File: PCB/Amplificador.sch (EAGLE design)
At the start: 36 parts, among them Q1 BC214, Q10 MJE2955, Q11 MJE3055, Q2 BC214, Q3 BC214, Q4 BC214, Q5 2N3904, Q6 2N3904, Q7 2N3904, Q8 2N3904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

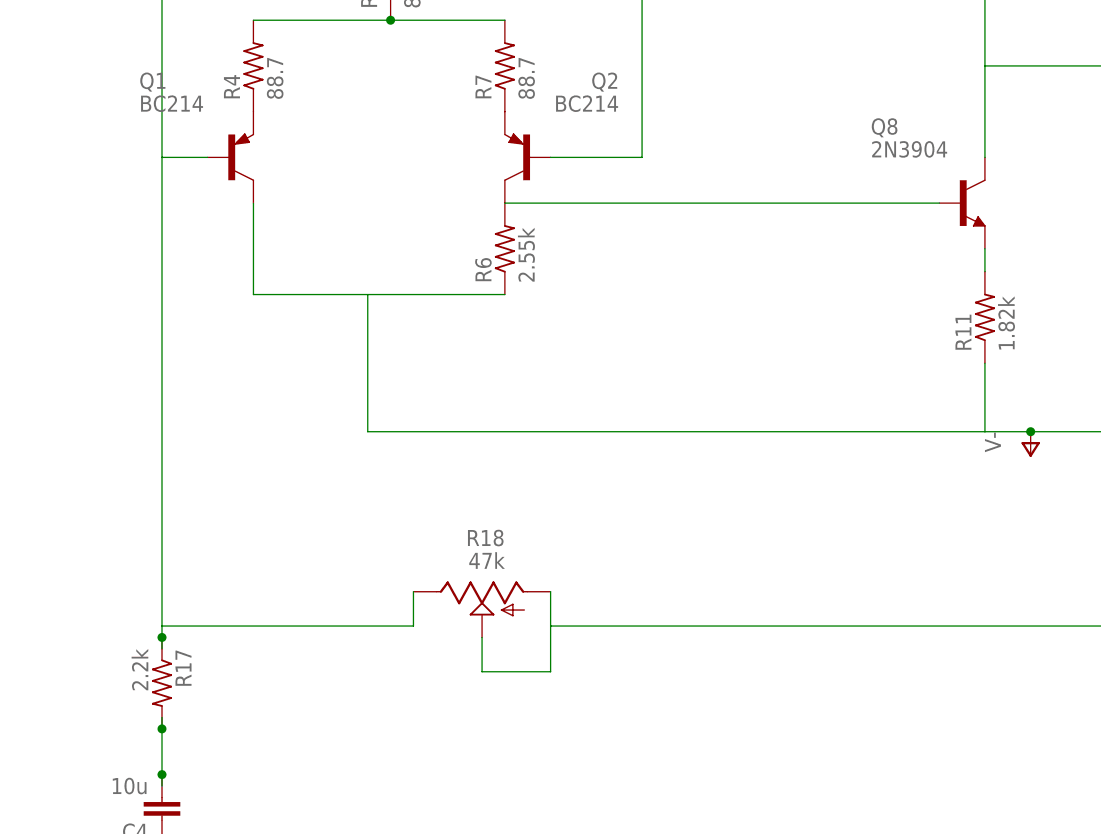
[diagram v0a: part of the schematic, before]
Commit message: Placa Versão 2.0
Talvez a versão final, compatível com nossos componentes comprados
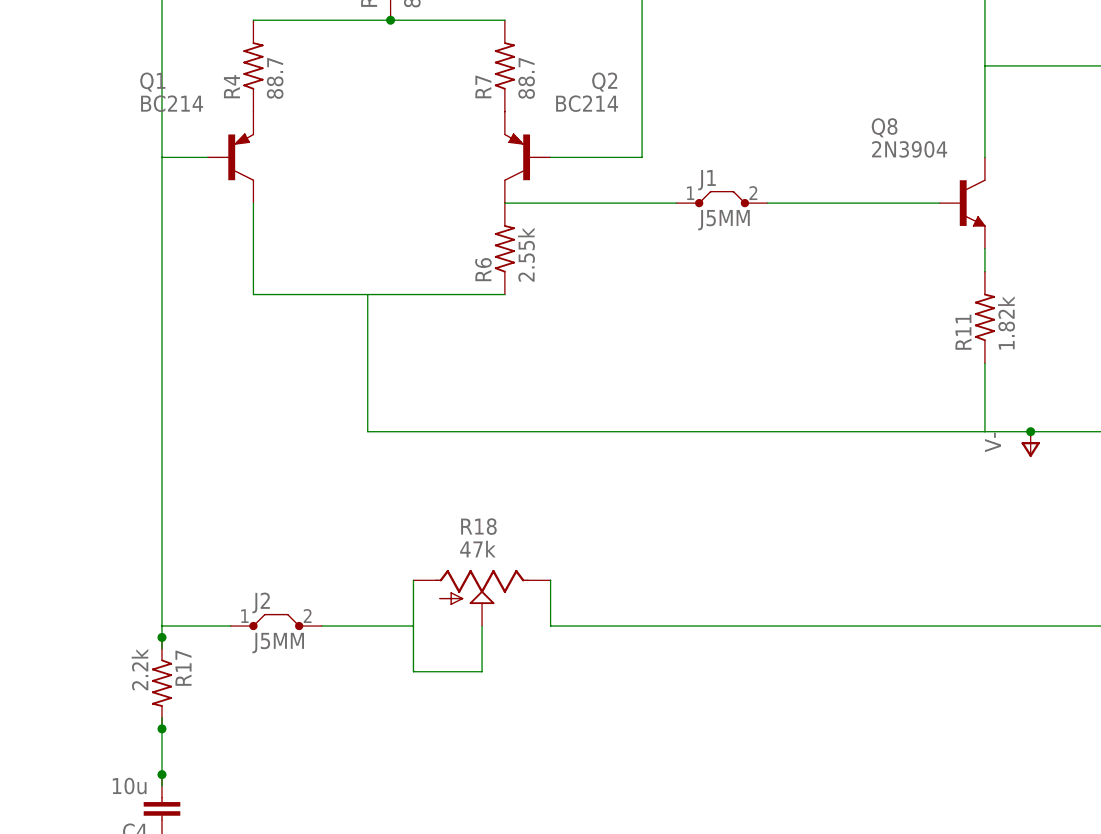
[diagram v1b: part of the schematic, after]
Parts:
- added J1, J2: J5MM, jumper:J5MM
- R18: device pot:TRIM_US-CA6V -> pot:TRIM_US-CA6H
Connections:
- new net N$25: J1.1, Q2.C, R6.2
- new net N$26: J2.1, Q1.B, Q5.B, R17.1
- net N$15: now also R18.E; no longer R18.A, R18.S
- net N$19: now also J2.2, R18.A, R18.S; no longer Q1.B, Q5.B, R17.1, R18.E
- net N$2: now also J1.2; no longer Q2.C, R6.2
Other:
- moved on the sheet: R18
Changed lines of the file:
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@@
 <setting verticaltext="up"/>
 </settings>
-<grid distance="0.1" unitdist="inch" unit="inch" style="lines" multiple="1" display="no" altdistance="0.01" altunitdist="inch" altunit="inch"/>
+<grid distance="0.05" unitdist="inch" unit="inch" style="lines" multiple="1" display="no" altdistance="0.01" altunitdist="inch" altunit="inch"/>
 <layers>
 <layer number="1" name="Top" color="4" fill="1" visible="no" active="no"/>
+<layer number="2" name="Route2" color="1" fill="3" visible="no" active="no"/>
+<layer number="3" name="Route3" color="4" fill="3" visible="no" active="no"/>
+<layer number="4" name="Route4" color="1" fill="4" visible="no" active="no"/>
+<layer number="5" name="Route5" color="4" fill="4" visible="no" active="no"/>
+<layer number="6" name="Route6" color="1" fill="8" visible="no" active="no"/>
+<layer number="7" name="Route7" color="4" fill="8" visible="no" active="no"/>
+<layer number="8" name="Route8" color="1" fill="2" visible="no" active="no"/>
+<layer number="9" name="Route9" color="4" fill="2" visible="no" active="no"/>
+<layer number="10" name="Route10" color="1" fill="7" visible="no" active="no"/>
+<layer number="11" name="Route11" color="4" fill="7" visible="no" active="no"/>
+<layer number="12" name="Route12" color="1" fill="5" visible="no" active="no"/>
+<layer number="13" name="Route13" color="4" fill="5" visible="no" active="no"/>
+<layer number="14" name="Route14" color="1" fill="6" visible="no" active="no"/>
+<layer number="15" name="Route15" color="4" fill="6" visible="no" active="no"/>
 <layer number="16" name="Bottom" color="1" fill="1" visible="no" active="no"/>
 <layer number="17" name="Pads" color="2" fill="1" visible="no" active="no"/>
@@
 <part name="GND4" library="supply1" library_urn="urn:adsk.eagle:library:371" deviceset="GND" device=""/>
 <part name="R17" library="resistor" library_urn="urn:adsk.eagle:library:348" deviceset="R-US_" device="0207/10" package3d_urn="urn:adsk.eagle:package:25939/1" value="2.2k"/>
-<part name="R18" library="pot" library_urn="urn:adsk.eagle:library:331" deviceset="TRIM_US-" device="CA6V" package3d_urn="urn:adsk.eagle:package:22691/1" value="47k"/>
 <part name="C4" library="capacitor-wima" library_urn="urn:adsk.eagle:library:116" deviceset="C" device="5/2.5" package3d_urn="urn:adsk.eagle:package:5426/1" value="10u"/>
 <part name="GND5" library="supply1" library_urn="urn:adsk.eagle:library:371" deviceset="GND" device=""/>
@@
 <part name="Q10" library="transistor-power" library_urn="urn:adsk.eagle:library:400" deviceset="MJE2955" device="" package3d_urn="urn:adsk.eagle:package:29487/1"/>
 <part name="Q11" library="transistor-power" library_urn="urn:adsk.eagle:library:400" deviceset="MJE3055" device="" package3d_urn="urn:adsk.eagle:package:29487/1"/>
+<part name="J1" library="jumper" library_urn="urn:adsk.eagle:library:252" deviceset="J" device="5MM" package3d_urn="urn:adsk.eagle:package:15465/1"/>
+<part name="R18" library="pot" library_urn="urn:adsk.eagle:library:331" deviceset="TRIM_US-" device="CA6H" package3d_urn="urn:adsk.eagle:package:22689/1" value="47k"/>
+<part name="J2" library="jumper" library_urn="urn:adsk.eagle:library:252" deviceset="J" device="5MM" package3d_urn="urn:adsk.eagle:package:15465/1"/>
 </parts>
 <sheets>
@@
 <instance part="GND4" gate="1" x="-35.56" y="120.65"/>
 <instance part="R17" gate="G$1" x="-78.74" y="16.51" rot="R270"/>
-<instance part="R18" gate="G$1" x="-43.18" y="26.67" rot="MR270"/>
 <instance part="C4" gate="G$1" x="-78.74" y="1.27" rot="R180"/>
 <instance part="GND5" gate="1" x="-78.74" y="-16.51"/>
@@
 <instance part="Q10" gate="1" x="71.12" y="95.25"/>
 <instance part="Q11" gate="1" x="71.12" y="143.51"/>
+<instance part="J1" gate="1" x="-16.51" y="69.85"/>
+<instance part="R18" gate="G$1" x="-43.18" y="27.94" rot="R270"/>
+<instance part="J2" gate="1" x="-66.04" y="22.86"/>
 </instances>
 <busses>
@@
 <net name="N$2" class="0">
 <segment>
-<pinref part="R6" gate="G$1" pin="2"/>
-<pinref part="Q2" gate="G$1" pin="C"/>
 <pinref part="Q8" gate="G1" pin="B"/>
-<wire x1="-40.64" y1="69.85" x2="7.62" y2="69.85" width="0.1524" layer="91"/>
+<pinref part="J1" gate="1" pin="2"/>
+<wire x1="-11.43" y1="69.85" x2="7.62" y2="69.85" width="0.1524" layer="91"/>
 </segment>
 </net>
@@
 <net name="N$15" class="0">
 <segment>
-<wire x1="-43.18" y1="21.59" x2="-43.18" y2="17.78" width="0.1524" layer="91"/>
-<wire x1="-43.18" y1="17.78" x2="-35.56" y2="17.78" width="0.1524" layer="91"/>
-<wire x1="-35.56" y1="22.86" x2="-35.56" y2="26.67" width="0.1524" layer="91"/>
-<wire x1="-35.56" y1="17.78" x2="-35.56" y2="22.86" width="0.1524" layer="91"/>
+<wire x1="-35.56" y1="22.86" x2="-35.56" y2="27.94" width="0.1524" layer="91"/>
 <wire x1="73.66" y1="123.19" x2="73.66" y2="118.11" width="0.1524" layer="91"/>
 <pinref part="R13" gate="G$1" pin="1"/>
@@
 <wire x1="104.14" y1="22.86" x2="104.14" y2="118.11" width="0.1524" layer="91"/>
 <wire x1="-35.56" y1="22.86" x2="104.14" y2="22.86" width="0.1524" layer="91"/>
-<pinref part="R18" gate="G$1" pin="A"/>
-<pinref part="R18" gate="G$1" pin="S"/>
+<pinref part="R18" gate="G$1" pin="E"/>
 </segment>
 </net>
@@
 </segment>
 </net>
-<net name="N$19" class="0">
-<segment>
-<pinref part="R18" gate="G$1" pin="E"/>
-<wire x1="-50.8" y1="22.86" x2="-50.8" y2="26.67" width="0.1524" layer="91"/>
+<net name="N$25" class="0">
+<segment>
+<pinref part="J1" gate="1" pin="1"/>
+<pinref part="R6" gate="G$1" pin="2"/>
+<pinref part="Q2" gate="G$1" pin="C"/>
+<wire x1="-40.64" y1="69.85" x2="-21.59" y2="69.85" width="0.1524" layer="91"/>
+</segment>
+</net>
+<net name="N$26" class="0">
+<segment>
 <wire x1="-78.74" y1="20.32" x2="-78.74" y2="21.59" width="0.1524" layer="91"/>
 <pinref part="R17" gate="G$1" pin="1"/>
 <junction x="-78.74" y="21.59"/>
 <wire x1="-78.74" y1="21.59" x2="-78.74" y2="22.86" width="0.1524" layer="91"/>
-<wire x1="-78.74" y1="22.86" x2="-50.8" y2="22.86" width="0.1524" layer="91"/>
+<wire x1="-78.74" y1="22.86" x2="-71.12" y2="22.86" width="0.1524" layer="91"/>
 <pinref part="Q5" gate="G1" pin="B"/>
 <wire x1="-78.74" y1="151.13" x2="-71.12" y2="151.13" width="0.1524" layer="91"/>
@@
 <pinref part="Q1" gate="G$1" pin="B"/>
 <wire x1="-73.66" y1="74.93" x2="-78.74" y2="74.93" width="0.1524" layer="91"/>
-</segment>
-</net>
+<pinref part="J2" gate="1" pin="1"/>
+</segment>
+</net>
+<net name="N$19" class="0">
+<segment>
+<pinref part="R18" gate="G$1" pin="A"/>
+<wire x1="-50.8" y1="22.86" x2="-50.8" y2="27.94" width="0.1524" layer="91"/>
+<pinref part="J2" gate="1" pin="2"/>
+<wire x1="-60.96" y1="22.86" x2="-50.8" y2="22.86" width="0.1524" layer="91"/>
+<wire x1="-50.8" y1="17.78" x2="-50.8" y2="22.86" width="0.1524" layer="91"/>
+<wire x1="-43.18" y1="17.78" x2="-50.8" y2="17.78" width="0.1524" layer="91"/>
+<wire x1="-43.18" y1="22.86" x2="-43.18" y2="17.78" width="0.1524" layer="91"/>
+<pinref part="R18" gate="G$1" pin="S"/>
+</segment>
+</net>
